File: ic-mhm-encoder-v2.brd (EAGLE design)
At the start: 58 x 58.3 mm, 21 parts, among them J1 5040500291, J2 5040501191, M1 BSS670S2LH6327XTSA1, U1 24LC16BT-I/MC, U2 D5V0F4U6S-7, U3 D5V0F4U6S-7, U4 D5V0F4U6S-7, U6 UA9638CDR

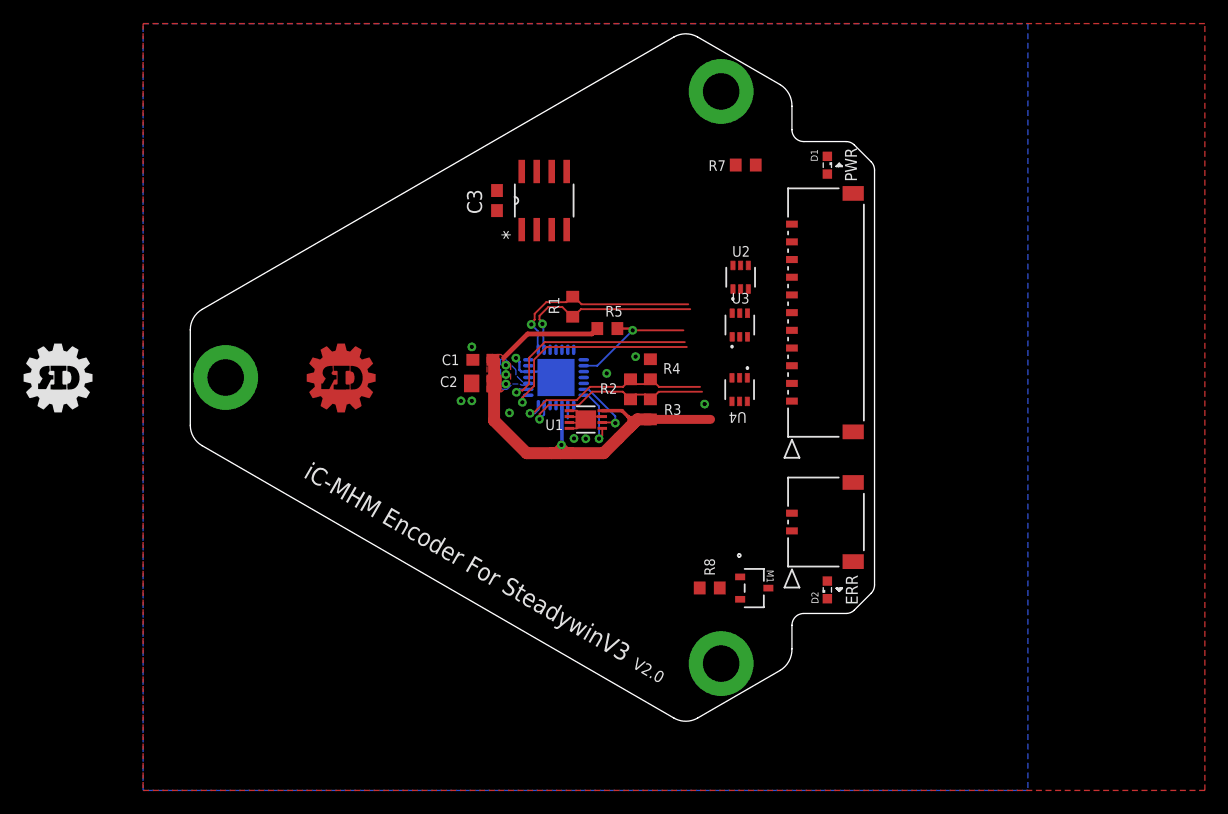
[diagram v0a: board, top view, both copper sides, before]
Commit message: Finished routing of v2 pcb, ready for design review
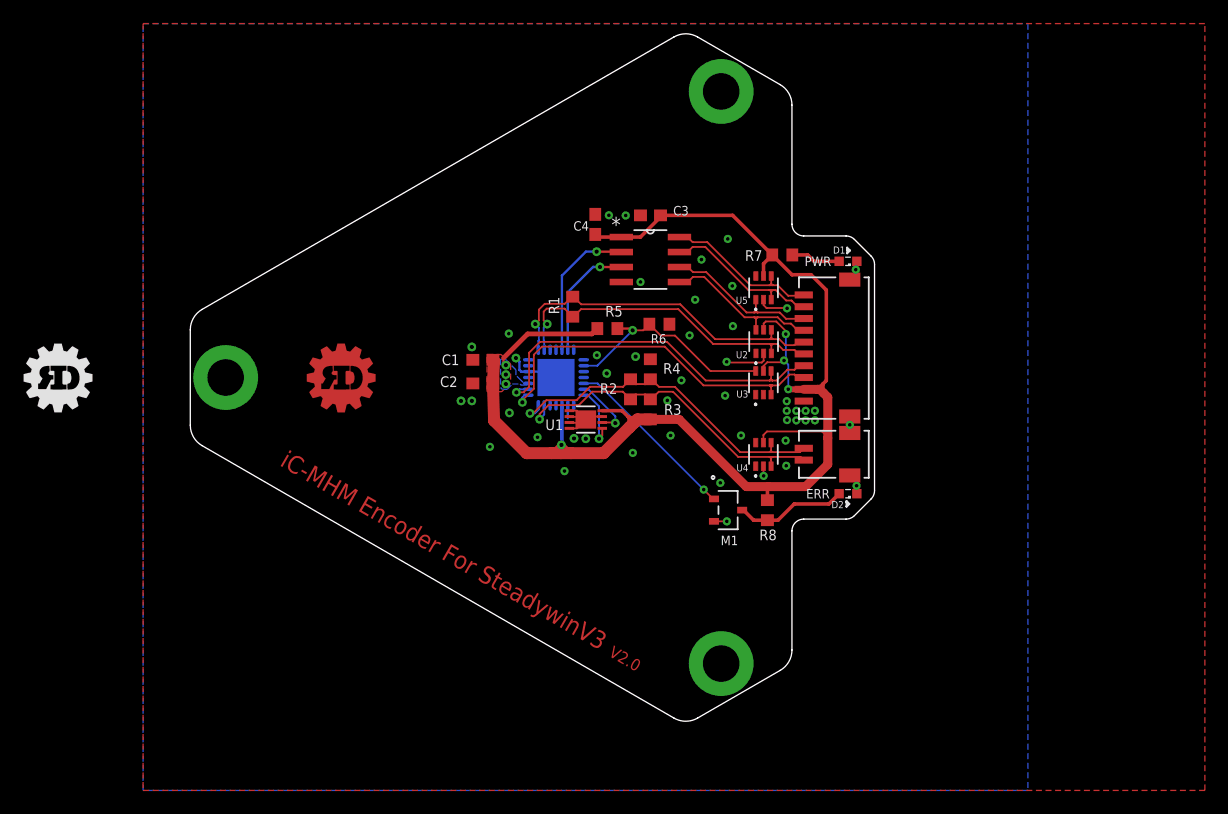
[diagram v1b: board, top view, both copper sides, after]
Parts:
- added C4: 10uF, rcl:C0603
- added R6: NP, rcl:R0603
- added U5: D5V0F4U6S-7, ic-mhm:SOT-363_DIO
- C2: device rcl:C0805 -> rcl:C0603
- J1: value 5040500291 -> 2023960207; device ic-mhm:CON_5040500291 -> ic-mhm:CON_2023960207
- J2: value 5040501191 -> 2023961007; device ic-mhm:CON_5040501191 -> ic-mhm:CON_2023961007
- moved C3 13.1 mm to (8.01, 13.7), turned to 180 degrees
- moved U6 10.3 mm to (8.00, 10.0), turned to 0 degrees
- moved D1 8.34 mm to (24.8, 9.85), turned to 180 degrees
- moved D2 8.34 mm to (24.8, -9.85), turned to 180 degrees
- moved R7 8.23 mm to (19.2, 10.4)
- moved R8 8.21 mm to (17.9, -11.2), turned to 270 degrees
- moved M1 6.97 mm to (14.6, -11.2)
- moved J1 6.08 mm to (21.0, -7.00), turned to 90 degrees
- moved U4 5.85 mm to (17.6, -6.52), turned to 90 degrees
- moved U2 5.79 mm to (17.6, 3.04)
- moved U3 5.29 mm to (17.6, -0.45)
- moved J2 1.00 mm to (21.0, -2.00), turned to 90 degrees
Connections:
- removed net !DN: U4.3
- removed net !UP: U4.1
- removed net ENC_A: U4.6
- removed net ENC_B: U2.6
- removed net N$3: U6.8
- removed net N$7: U6.7
- removed net N$8: U6.6
- removed net N$9: U6.5
- removed net VCC: C3.1, U6.1
- new net ENC_A_N: J2.9, U5.3, U6.7
- new net ENC_A_P: J2.10, U5.4, U6.8
- new net ENC_B_N: J2.7, U2.6, U6.5
- new net ENC_B_P: J2.8, U5.1, U6.6
- net GND: now also C4.2, J1.3, J1.4, J2.1, J2.11, J2.12, R6.1, U5.2
- net MA_N: now also J2.5
- net MA_P: now also J2.6
- net NCS: now also R6.2
- net SLI_N: now also J1.1, U4.3; no longer U4.4
- net SLI_P: now also J1.2, U4.4; no longer U3.1
- net SLO_N: now also J2.3
- net SLO_P: now also J2.4
- net VDD: now also C3.1, C4.1, J2.2, U5.5, U6.1
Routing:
- net VDD: track 48.5 -> 123.5 mm, vias 4 -> 7
- net NERR: track 0.00 -> 15.1 mm, vias 0 -> 1
- net ENC_B_N: track 0.00 -> 13.9 mm
- net ENC_A_N: track 0.00 -> 13.9 mm
- net ENC_B_P: track 0.00 -> 13.7 mm
- net ENC_A_P: track 0.00 -> 13.6 mm
- net SLO_P: track 18.4 -> 31.8 mm
- net SLO_N: track 18.4 -> 31.7 mm
- net SLI_P: track 17.4 -> 29.7 mm
- net ENC_A_MHM: track 0.00 -> 12.2 mm, vias 0 -> 1
- net MA_P: track 17.3 -> 29.4 mm
- net MA_N: track 16.7 -> 28.8 mm
- net SLI_N: track 17.2 -> 29.2 mm
- net ENC_B_MHM: track 0.00 -> 10.3 mm, vias 0 -> 1
- net N$5: track 0.00 -> 9.51 mm
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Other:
- outline, holes or cut-outs redrawn
- board text added: "A+ A- B+ B- MA NMA SLO NSLO 5V GND"
- board text removed: "A+ A- B+ B- MA NMA NCS SLO NSLO 5V GND"

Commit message: added zip tie slots
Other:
- board size 58 x 58.3 mm -> 63 x 58.3 mm
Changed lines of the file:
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@@
 <wire x1="20" y1="-23.09401875" x2="20" y2="-13" width="0" layer="20"/>
 <wire x1="20" y1="-13" x2="21" y2="-12" width="0" layer="20" curve="-90"/>
-<wire x1="21" y1="-12" x2="24.5857875" y2="-12" width="0" layer="20"/>
-<wire x1="24.5857875" y1="-12" x2="25.29289375" y2="-11.70710625" width="0" layer="20" curve="45"/>
-<wire x1="25.29289375" y1="-11.70710625" x2="26.70710625" y2="-10.29289375" width="0" layer="20"/>
-<wire x1="26.70710625" y1="-10.29289375" x2="27" y2="-9.5857875" width="0" layer="20" curve="45"/>
-<wire x1="27" y1="-9.5857875" x2="27" y2="9.5857875" width="0" layer="20"/>
-<wire x1="27" y1="9.5857875" x2="26.70710625" y2="10.29289375" width="0" layer="20" curve="45"/>
-<wire x1="26.70710625" y1="10.29289375" x2="25.29289375" y2="11.70710625" width="0" layer="20"/>
-<wire x1="25.29289375" y1="11.70710625" x2="24.5857875" y2="12" width="0" layer="20" curve="45"/>
-<wire x1="24.5857875" y1="12" x2="21" y2="12" width="0" layer="20"/>
+<wire x1="21" y1="-12" x2="25.171571875" y2="-12" width="0" layer="20"/>
+<wire x1="25.171571875" y1="-12" x2="26.5857875" y2="-11.4142125" width="0" layer="20" curve="45.000063"/>
+<wire x1="26.5857875" y1="-11.4142125" x2="31.4142125" y2="-6.5857875" width="0" layer="20"/>
+<wire x1="31.4142125" y1="-6.5857875" x2="32" y2="-5.171571875" width="0" layer="20" curve="45.00009"/>
+<wire x1="32" y1="-5.171571875" x2="32" y2="5.171571875" width="0" layer="20"/>
+<wire x1="32" y1="5.171571875" x2="31.4142125" y2="6.5857875" width="0" layer="20" curve="45.000063"/>
+<wire x1="31.4142125" y1="6.5857875" x2="26.5857875" y2="11.4142125" width="0" layer="20"/>
+<wire x1="26.5857875" y1="11.4142125" x2="25.171571875" y2="12" width="0" layer="20" curve="45.00009"/>
+<wire x1="25.171571875" y1="12" x2="21" y2="12" width="0" layer="20"/>
 <wire x1="21" y1="12" x2="20" y2="13" width="0" layer="20" curve="-90"/>
 <circle x="0" y="0" radius="37.5" width="0.1016" layer="51"/>
@@
 <rectangle x1="-42.53895" y1="2.86705" x2="-41.89125" y2="2.87975" layer="21"/>
 <text x="7.0748" y="-24.53" size="1" layer="29" font="vector" ratio="12" rot="R330" align="center-right">V2.0</text>
-<text x="25.5748" y="2.3556" size="0.8" layer="22" font="vector" distance="25" rot="MR0" align="center-left">A+
+<text x="25.6002" y="2.4826" size="0.8" layer="22" font="vector" distance="25" rot="MR0" align="center-left">A+
 A-
 B+
@@
 <text x="4.1218" y="-22.4934" size="1.5" layer="1" font="vector" rot="R330" align="center-right">iC-MHM Encoder For SteadywinV3</text>
 <text x="7.0748" y="-24.53" size="1" layer="1" font="vector" rot="R330" align="center-right">V2.0</text>
+<wire x1="28.9" y1="6" x2="30.1" y2="6" width="0" layer="20"/>
+<wire x1="30.1" y1="6" x2="31" y2="5.1" width="0" layer="20" curve="-90"/>
+<wire x1="31" y1="5.1" x2="31" y2="4.9" width="0" layer="20"/>
+<wire x1="31" y1="4.9" x2="30.1" y2="4" width="0" layer="20" curve="-90"/>
+<wire x1="30.1" y1="4" x2="28.9" y2="4" width="0" layer="20"/>
+<wire x1="28.9" y1="4" x2="28" y2="4.9" width="0" layer="20" curve="-90"/>
+<wire x1="28" y1="4.9" x2="28" y2="5.1" width="0" layer="20"/>
+<wire x1="28" y1="5.1" x2="28.9" y2="6" width="0" layer="20" curve="-90"/>
+<wire x1="30.1" y1="1" x2="28.9" y2="1" width="0" layer="20"/>
+<wire x1="28.9" y1="1" x2="28" y2="0.1" width="0" layer="20" curve="90"/>
+<wire x1="28" y1="0.1" x2="28" y2="-0.1" width="0" layer="20"/>
+<wire x1="28" y1="-0.1" x2="28.9" y2="-1" width="0" layer="20" curve="90"/>
+<wire x1="28.9" y1="-1" x2="30.1" y2="-1" width="0" layer="20"/>
+<wire x1="30.1" y1="-1" x2="31" y2="-0.1" width="0" layer="20" curve="90"/>
+<wire x1="31" y1="-0.1" x2="31" y2="0.1" width="0" layer="20"/>
+<wire x1="31" y1="0.1" x2="30.1" y2="1" width="0" layer="20" curve="90"/>
 </plain>
 <attributes>

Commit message: added mfg and assembly files for v2
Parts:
- removed R6: NP, rcl:R0603
- added FID1, FID2, FID3, FID4, FID5, FID6, FID7, FID8: FIDUCIAL_1MM, microbuilder:FIDUCIAL_1MM
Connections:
- net GND: no longer R6.1
- net NCS: no longer R6.2
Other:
- board text added: "U7"
